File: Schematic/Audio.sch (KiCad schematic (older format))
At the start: 4 parts

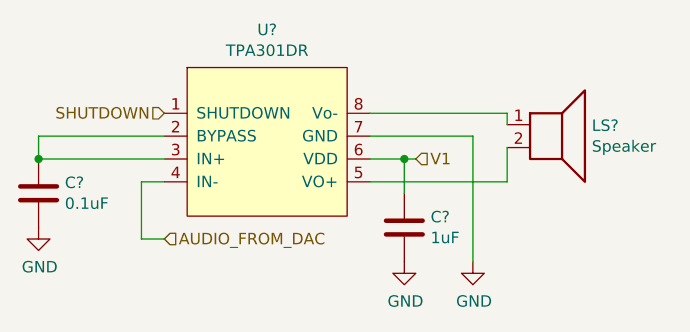
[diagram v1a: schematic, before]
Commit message: Perform annotation start assigning footprints
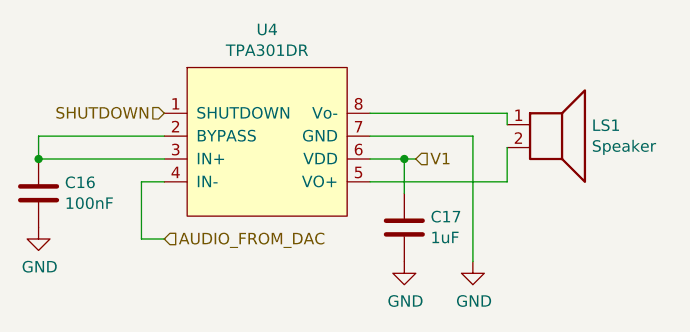
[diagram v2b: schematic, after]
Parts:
- C16: renamed from C?; value 0.1uF -> 100nF; footprint (none) -> Capacitor_SMD:C_0603_1608Metric_Pad1.05x0.95mm_HandSolder
- C17: renamed from C?; footprint (none) -> Capacitor_SMD:C_0603_1608Metric_Pad1.05x0.95mm_HandSolder
- U4: renamed from U?; footprint (none) -> Package_SO:SOIC-8-N7_3.9x4.9mm_P1.27mm
- gave numbers to parts that had none: 1
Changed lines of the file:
@@
 P 3350 2050
 AR Path="/5E238EA5/5E27BD61" Ref="U?"  Part="1"
-AR Path="/5E27AF1B/5E27BD61" Ref="U?"  Part="1"
+AR Path="/5E27AF1B/5E27BD61" Ref="U4"  Part="1"
 AR Path="/5E27BE41/5E27BD61" Ref="U?"  Part="1"
-F 0 "U?" H 3350 2265 50  0000 C CNN
+F 0 "U4" H 3350 2265 50  0000 C CNN
 F 1 "TPA301DR" H 3350 2174 50  0000 C CNN
-F 2 "" H 3350 2050 50  0001 C CNN
+F 2 "Package_SO:SOIC-8-N7_3.9x4.9mm_P1.27mm" H 3350 2050 50  0001 C CNN
 F 3 "" H 3350 2050 50  0001 C CNN
 	1    3350 2050
@@
 $EndComp
 $Comp
-L Device:Speaker LS?
+L Device:Speaker LS1
 U 1 1 5E292C02
 P 4600 2250
-F 0 "LS?" H 4770 2246 50  0000 L CNN
+F 0 "LS1" H 4770 2246 50  0000 L CNN
 F 1 "Speaker" H 4770 2155 50  0000 L CNN
 F 2 "" H 4600 2050 50  0001 C CNN
@@
 	4400 2200 4400 2250
 $Comp
-L Device:C C?
+L Device:C C17
 U 1 1 5E292D43
 P 3950 2700
-F 0 "C?" H 4065 2746 50  0000 L CNN
+F 0 "C17" H 4065 2746 50  0000 L CNN
 F 1 "1uF" H 4065 2655 50  0000 L CNN
-F 2 "" H 3988 2550 50  0001 C CNN
+F 2 "Capacitor_SMD:C_0603_1608Metric_Pad1.05x0.95mm_HandSolder" H 3988 2550 50  0001 C CNN
 F 3 "~" H 3950 2700 50  0001 C CNN
 	1    3950 2700
@@
 SHUTDOWN
 $Comp
-L Device:C C?
+L Device:C C16
 U 1 1 5E293160
 P 2350 2550
-F 0 "C?" H 2465 2596 50  0000 L CNN
-F 1 "0.1uF" H 2465 2505 50  0000 L CNN
-F 2 "" H 2388 2400 50  0001 C CNN
+F 0 "C16" H 2465 2596 50  0000 L CNN
+F 1 "100nF" H 2465 2505 50  0000 L CNN
+F 2 "Capacitor_SMD:C_0603_1608Metric_Pad1.05x0.95mm_HandSolder" H 2388 2400 50  0001 C CNN
 F 3 "~" H 2350 2550 50  0001 C CNN
 	1    2350 2550

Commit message: Selected components
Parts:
- LS1: footprint (none) -> Soundboard:speaker_pads
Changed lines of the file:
@@
 EESchema Schematic File Version 4
-LIBS:SoundBoard-cache
-EELAYER 26 0
+EELAYER 30 0
 EELAYER END
 $Descr A4 11693 8268
@@
 F 0 "LS1" H 4770 2246 50  0000 L CNN
 F 1 "Speaker" H 4770 2155 50  0000 L CNN
-F 2 "" H 4600 2050 50  0001 C CNN
+F 2 "Soundboard:speaker_pads" H 4600 2050 50  0001 C CNN
 F 3 "~" H 4590 2200 50  0001 C CNN
 	1    4600 2250

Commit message: Add i2c pullups and start placement
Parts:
- U4: footprint Package_SO:SOIC-8-N7_3.9x4.9mm_P1.27mm -> Package_SO:SOIC-8_3.9x4.9mm_P1.27mm
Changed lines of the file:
@@
 F 0 "U4" H 3350 2265 50  0000 C CNN
 F 1 "TPA301DR" H 3350 2174 50  0000 C CNN
-F 2 "Package_SO:SOIC-8-N7_3.9x4.9mm_P1.27mm" H 3350 2050 50  0001 C CNN
+F 2 "Package_SO:SOIC-8_3.9x4.9mm_P1.27mm" H 3350 2050 50  0001 C CNN
 F 3 "" H 3350 2050 50  0001 C CNN
 	1    3350 2050
